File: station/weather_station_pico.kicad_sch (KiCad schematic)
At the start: 26 parts, among them J1 Conn_01x03, J2 1984617, J3 STEMMA, J4 STEMMA_QT, J5 DS18B20, J6 1X7_HEADER, J7 73412-0110, J8 RJ11, J9 RJ11, U1 PICO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

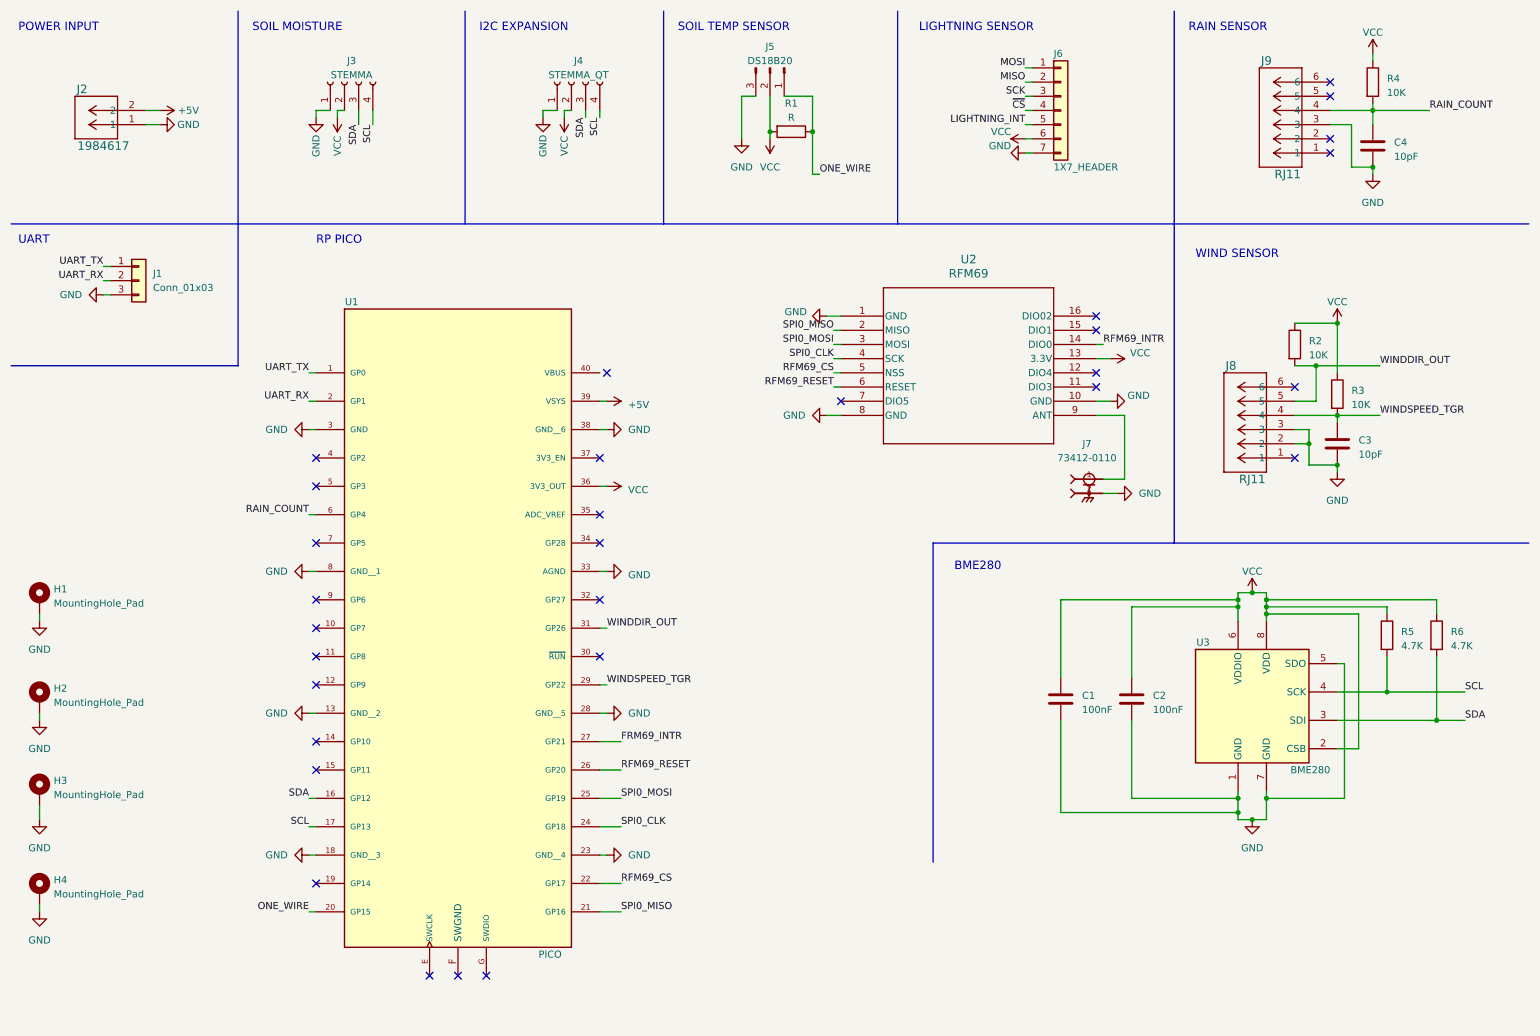
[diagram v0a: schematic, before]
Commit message: Updated the weather stations components
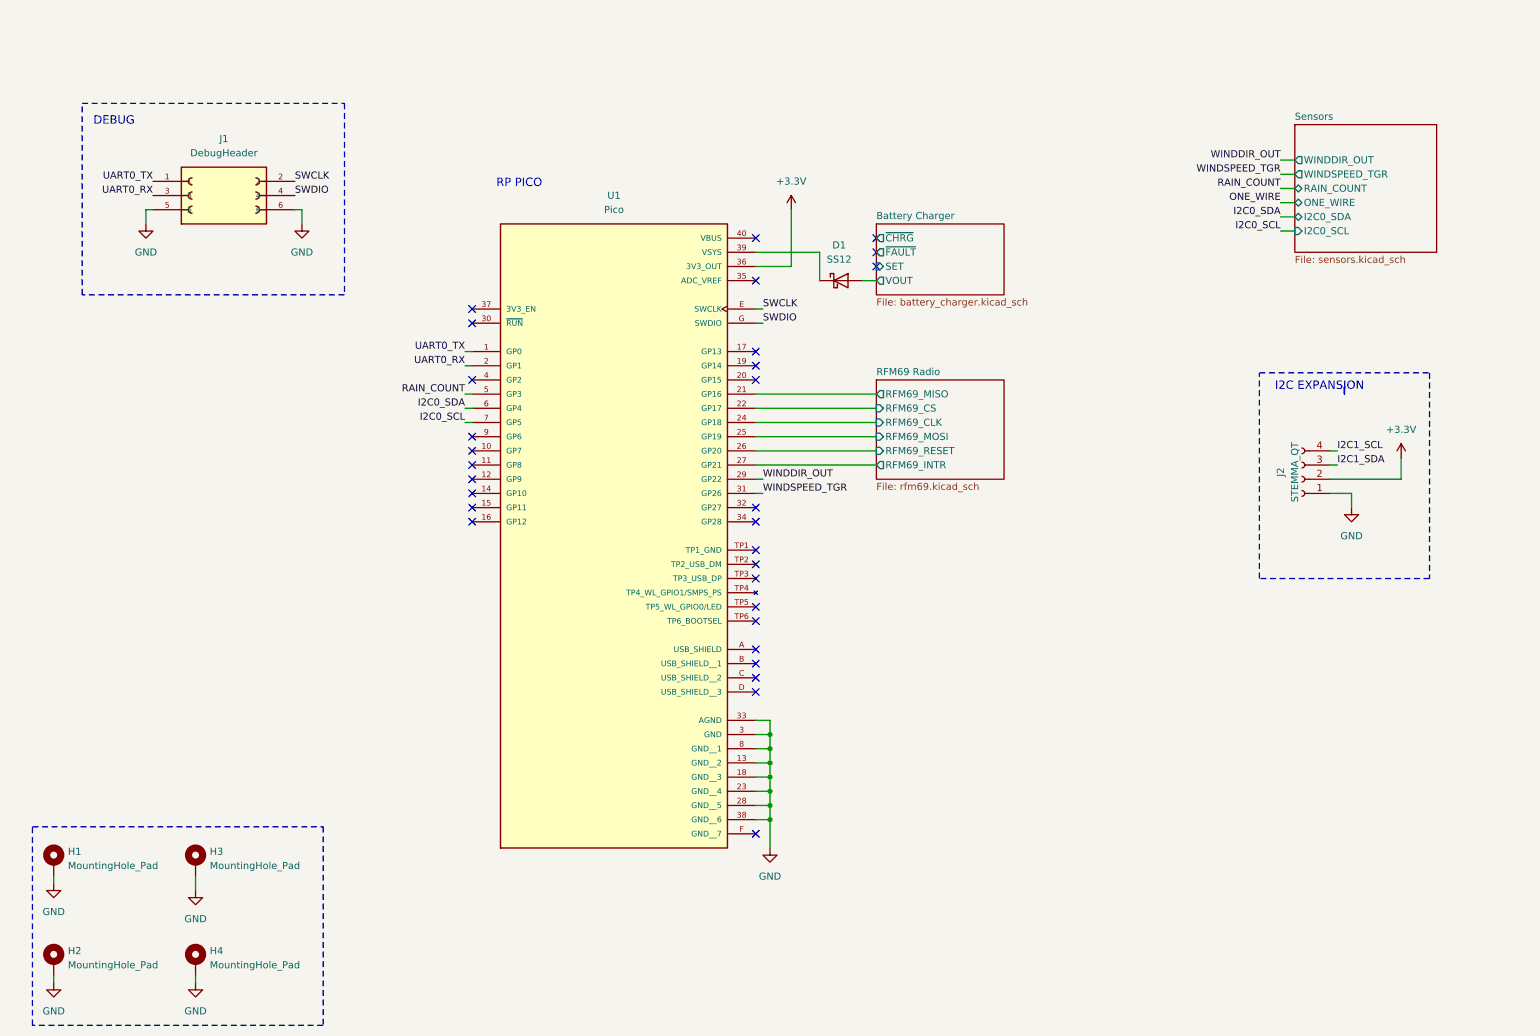
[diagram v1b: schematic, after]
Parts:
- removed C1, C2: 100nF, Capacitor_SMD:C_0805_2012Metric_Pad1.18x1.45mm_HandSolder, symbol Device:C
- removed C3, C4: 10pF, Capacitor_SMD:C_0805_2012Metric_Pad1.18x1.45mm_HandSolder, symbol Device:C
- removed J1: Conn_01x03, Connector_PinHeader_2.54mm:PinHeader_1x03_P2.54mm_Vertical, symbol Connector_Generic:Conn_01x03
- removed J2: 1984617, WeatherStation:CONN_1984617_PXC, symbol Weather_Sensors:1984617
- removed J3: STEMMA, WeatherStation:STEMMA_LARGE, symbol Connector:Conn_01x04_Socket
- removed J5: DS18B20, WeatherStation:STEMMA_LARGE_3pin, symbol Connector:Conn_01x03_Pin
- removed J6: 1X7_HEADER, Connector_PinHeader_2.54mm:PinHeader_1x07_P2.54mm_Vertical, symbol Connector_Generic:Conn_01x07
- removed J7: 73412-0110, 734120110:MOLEX_73412-0110, symbol 73412-0110:73412-0110
- removed J8, J9: RJ11, WeatherStation:CONN6_5555165-1_TEC, symbol Weather_Sensors:5555165-1
- removed R1: R, Resistor_SMD:R_0805_2012Metric_Pad1.20x1.40mm_HandSolder, symbol Device:R
- removed R2, R3, R4: 10K, Resistor_SMD:R_0805_2012Metric_Pad1.20x1.40mm_HandSolder, symbol Device:R
- removed R5, R6: 4.7K, Resistor_SMD:R_0805_2012Metric_Pad1.20x1.40mm_HandSolder, symbol Device:R
- removed U1: PICO, WeatherStation:PinHeader_2x20_P2.54mm_Vertical, symbol PicoW:SC0918
- removed U2: RFM69, RFM69:RFM69HCW_SPK, symbol 2024-03-24_21-06-40:COM-13909
- removed U3: BME280, Package_LGA:Bosch_LGA-8_2.5x2.5mm_P0.65mm_ClockwisePinNumbering, symbol Sensor:BME280
- added D1: SS12, Diode_SMD:D_SMA, symbol Diode:SS12
- added J1: DebugHeader, WeatherStation:DebugHeader, symbol Weather_Sensors:DebugHeader
- added U1: Pico, WeatherStation:MODULE_SC918_PINS, symbol Weather_Sensors:Pico W
- renumbered J4 to J2
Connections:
- net GND: now also J1.5, J1.6, U1.13 (GND__2), U1.18 (GND__3), U1.23 (GND__4), U1.28 (GND__5), U1.3 (GND), U1.33 (AGND), U1.38 (GND__6), U1.8 (GND__1)
- net RAIN_COUNT: now also U1.5 (GP3)
- net WINDDIR_OUT: now also U1.29 (GP22)
- net WINDSPEED_TGR: now also U1.31 (GP26)
- net SCL renamed I2C1_SCL
- net SDA renamed I2C1_SDA
- net VCC renamed +3.3V
- net +3.3V: now also U1.36 (3V3_OUT)
- new net: D1.1 (K), U1.39 (VSYS)
- new net Battery Charger/VOUT: D1.2 (A)
- new net I2C0_SCL: U1.7 (GP5)
- new net I2C0_SDA: U1.6 (GP4)
- new net RFM69 Radio/RFM69_CLK: U1.24 (GP18)
- new net RFM69 Radio/RFM69_CS: U1.22 (GP17)
- new net RFM69 Radio/RFM69_INTR: U1.27 (GP21)
- new net RFM69 Radio/RFM69_MISO: U1.21 (GP16)
- new net RFM69 Radio/RFM69_MOSI: U1.25 (GP19)
- new net RFM69 Radio/RFM69_RESET: U1.26 (GP20)
- new net SWCLK: J1.2, U1.E (SWCLK)
- new net SWDIO: J1.4, U1.G (SWDIO)
- new net UART0_RX: J1.3, U1.2 (GP1)
- new net UART0_TX: J1.1, U1.1 (GP0)
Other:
- added sheet Battery Charger (battery_charger.kicad_sch)
- added sheet RFM69 Radio (rfm69.kicad_sch)
- added sheet Sensors (sensors.kicad_sch)
- note added: "DEBUG"
- note removed: "BME280"
- note removed: "LIGHTNING SENSOR"
- note removed: "POWER INPUT"
- note removed: "RAIN SENSOR"
- note removed: "SOIL MOISTURE"
- note removed: "SOIL TEMP SENSOR"
- note removed: "UART"
- note removed: "WIND SENSOR"
- moved on the sheet: H1, H2, H3, H4, J2

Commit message: Signed-off-by: Scott Perkins <whatisbyandby@gmail.com>
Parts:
- U1: footprint WeatherStation:MODULE_SC918_PINS -> WeatherStation:Pico_SMD_Headers
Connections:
- net Battery Charger/VOUT renamed Battery Charger/Load+
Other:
- sheet Battery Charger ports: added Load+, Load-; removed VOUT
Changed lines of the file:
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@@
+	(wire
+		(pts
+			(xy 165.1 63.5) (xy 165.1 64.77)
+		)
+		(stroke
+			(width 0)
+			(type default)
+		)
+	)
 	(wire
 		(pts
@@
 		(pts
 			(xy 148.59 142.24) (xy 148.59 144.78)
+		)
+		(stroke
+			(width 0)
+			(type default)
+		)
+	)
+	(wire
+		(pts
+			(xy 167.64 63.5) (xy 165.1 63.5)
 		)
 		(stroke
@@
 	)
 	(symbol
+		(lib_name "GND_4")
+		(lib_id "power:GND")
+		(at 165.1 64.77 0)
+		(unit 1)
+		(exclude_from_sim no)
+		(in_bom yes)
+		(on_board yes)
+		(dnp no)
+		(fields_autoplaced yes)
+		(property "Reference" "#PWR025"
+			(at 165.1 71.12 0)
+			(effects
+				(font
+					(size 1.27 1.27)
+				)
+				(hide yes)
+			)
+		)
+		(property "Value" "GND"
+			(at 165.1 69.85 0)
+			(effects
+				(font
+					(size 1.27 1.27)
+				)
+			)
+		)
+		(property "Footprint" ""
+			(at 165.1 64.77 0)
+			(effects
+				(font
+					(size 1.27 1.27)
+				)
+				(hide yes)
+			)
+		)
+		(property "Datasheet" ""
+			(at 165.1 64.77 0)
+			(effects
+				(font
+					(size 1.27 1.27)
+				)
+				(hide yes)
+			)
+		)
+		(property "Description" "Power symbol creates a global label with name \"GND\" , ground"
+			(at 165.1 64.77 0)
+			(effects
+				(font
+					(size 1.27 1.27)
+				)
+				(hide yes)
+			)
+		)
+		(pin "1"
+		)
+		(instances
+			(project "weather_station_pico"
+				(path "/8f1f45aa-e764-4c95-a223-c466cf9a95bf"
+					(reference "#PWR025")
+					(unit 1)
+				)
+			)
+		)
+	)
+	(symbol
 		(lib_id "Mechanical:MountingHole_Pad")
 		(at 20.32 182.88 0)
@@
 			)
 		)
-		(property "Footprint" "WeatherStation:MODULE_SC918_PINS"
+		(property "Footprint" "WeatherStation:Pico_SMD_Headers"
 			(at 120.65 93.98 0)
 			(effects
@@
 	(sheet
 		(at 167.64 50.8)
-		(size 22.86 12.7)
+		(size 22.86 17.78)
 		(fields_autoplaced yes)
 		(stroke
@@
 		)
 		(property "Sheetfile" "battery_charger.kicad_sch"
-			(at 167.64 64.0846 0)
+			(at 167.64 69.1646 0)
 			(effects
 				(font
@@
 			)
 		)
-		(pin "VOUT" output
+		(pin "Load+" passive
 			(at 167.64 60.96 180)
 			(effects
 				(font
+					(size 1.27 1.27)
+				)
+				(justify left)
+			)
+		)
+		(pin "Load-" passive
+			(at 167.64 63.5 180)
+			(effects
+				(font

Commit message: Reworked layout
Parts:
- removed J1: DebugHeader, WeatherStation:DebugHeader, symbol Weather_Sensors:DebugHeader
- J2: footprint WeatherStation:STEMMA_SMALL -> WeatherStation:STEMMA_LARGE
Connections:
- net LIGHT_INTR: now reaches U1.20 (GP15)
- net SWCLK: no longer names the net of U1.E (SWCLK)
- net SWDIO: no longer names the net of U1.G (SWDIO)
- net UART0_RX: no longer names the net of U1.2 (GP1)
- net UART0_TX: no longer names the net of U1.1 (GP0)
- no-connect marks 30 -> 33
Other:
- sheet Sensors ports: added LIGHT_INTR; removed none
- note removed: "DEBUG"

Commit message: Switched to a round board
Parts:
- added J2: I2C1_EXP, WeatherStation:StemmaQT_Vertical, symbol Connector:Conn_01x04_Socket
- added R1, R2, R3, R4: DNP, Resistor_SMD:R_0805_2012Metric_Pad1.20x1.40mm_HandSolder, symbol Device:R
- J1: renamed from J2; value STEMMA_QT -> I2C1_EXP; footprint WeatherStation:STEMMA_LARGE -> WeatherStation:StemmaQT_Vertical
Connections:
- net +3.3V: now also J2.2 (Pin_2), R1.1, R2.1, R3.1, R4.1
- net GND: now also J2.1 (Pin_1)
- net I2C0_SCL: now also J2.4 (Pin_4), R2.2
- net I2C0_SDA: now also J2.3 (Pin_3), R1.2
- net I2C1_SCL: now also U1.10 (GP7), R4.2
- net I2C1_SDA: now also U1.9 (GP6), R3.2
- net ONE_WIRE: now also U1.19 (GP14)
- no-connect marks 33 -> 30
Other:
- note added: "I2C Pull Up Resistors"
- moved on the sheet: H1, H2, H3, H4, J1

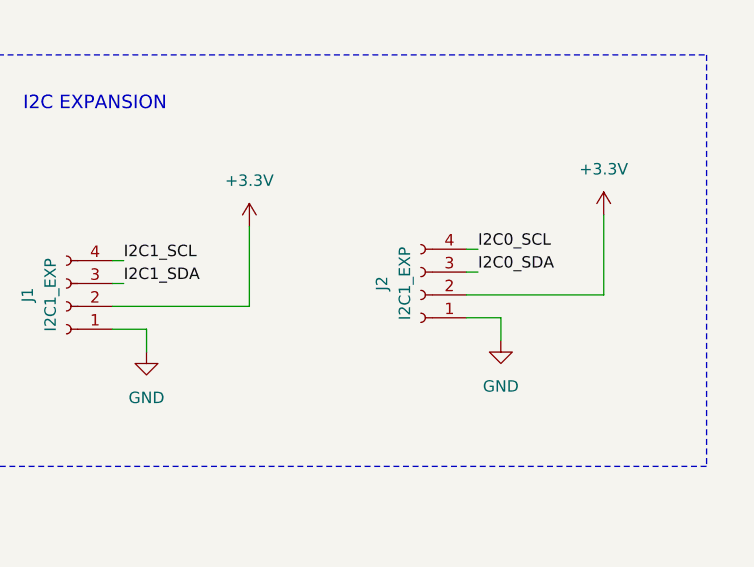
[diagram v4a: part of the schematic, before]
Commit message: Finished Square layout
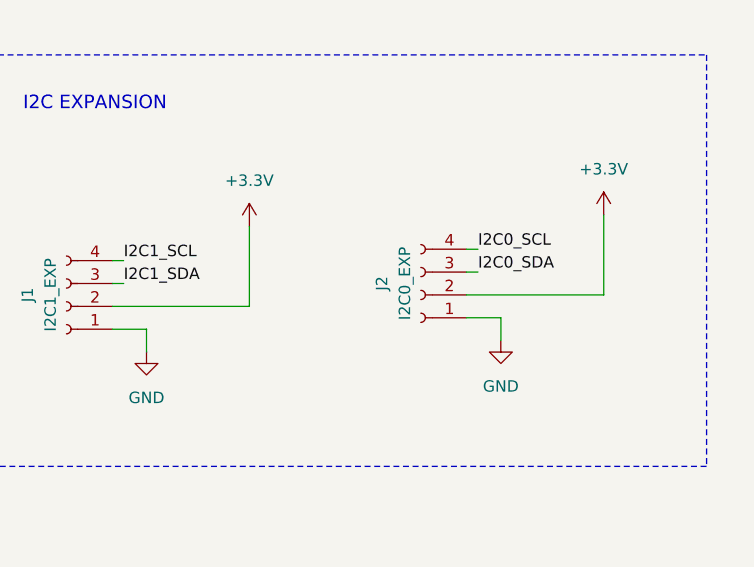
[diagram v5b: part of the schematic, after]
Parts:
- J2: value I2C1_EXP -> I2C0_EXP
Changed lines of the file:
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@@
 			)
 		)
-		(property "Value" "I2C1_EXP"
+		(property "Value" "I2C0_EXP"
 			(at 233.172 134.62 90)
 			(effects
